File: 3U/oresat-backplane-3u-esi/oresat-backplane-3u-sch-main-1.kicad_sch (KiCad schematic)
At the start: 30 parts

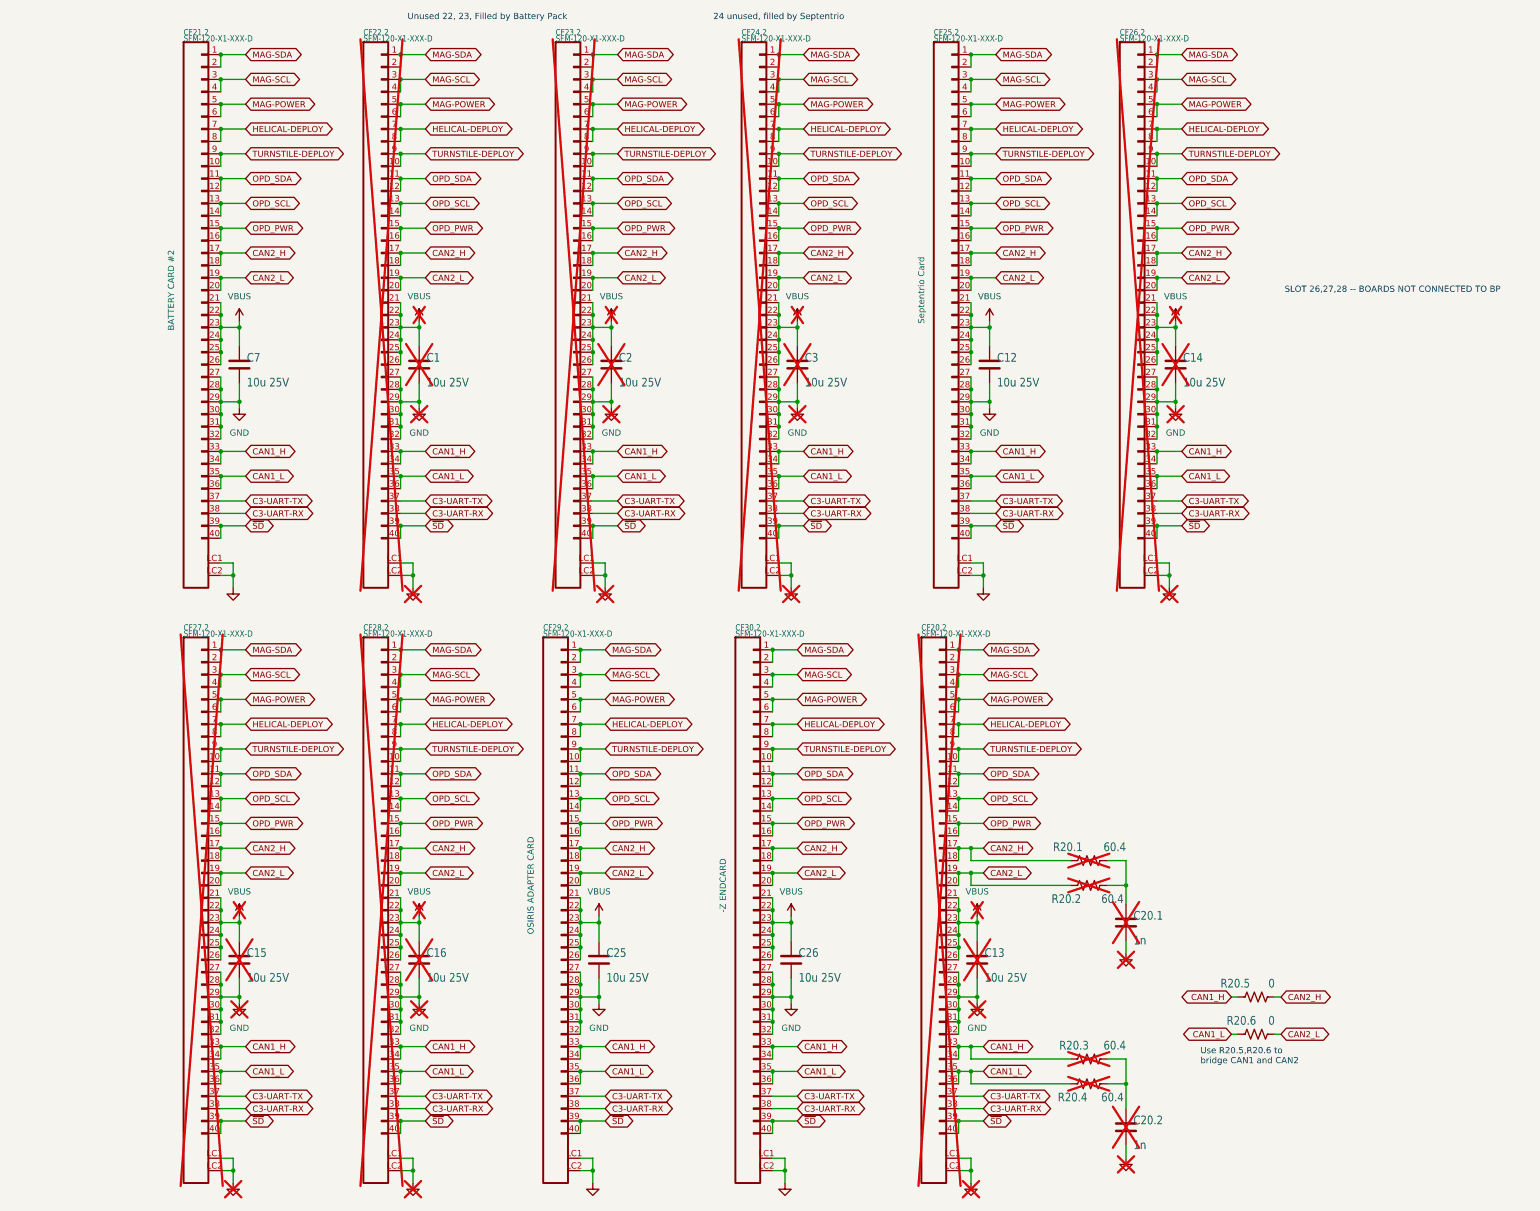
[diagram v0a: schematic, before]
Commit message: Added schematic and board variables, polished some silkscreen, reviewed board, renamed directory
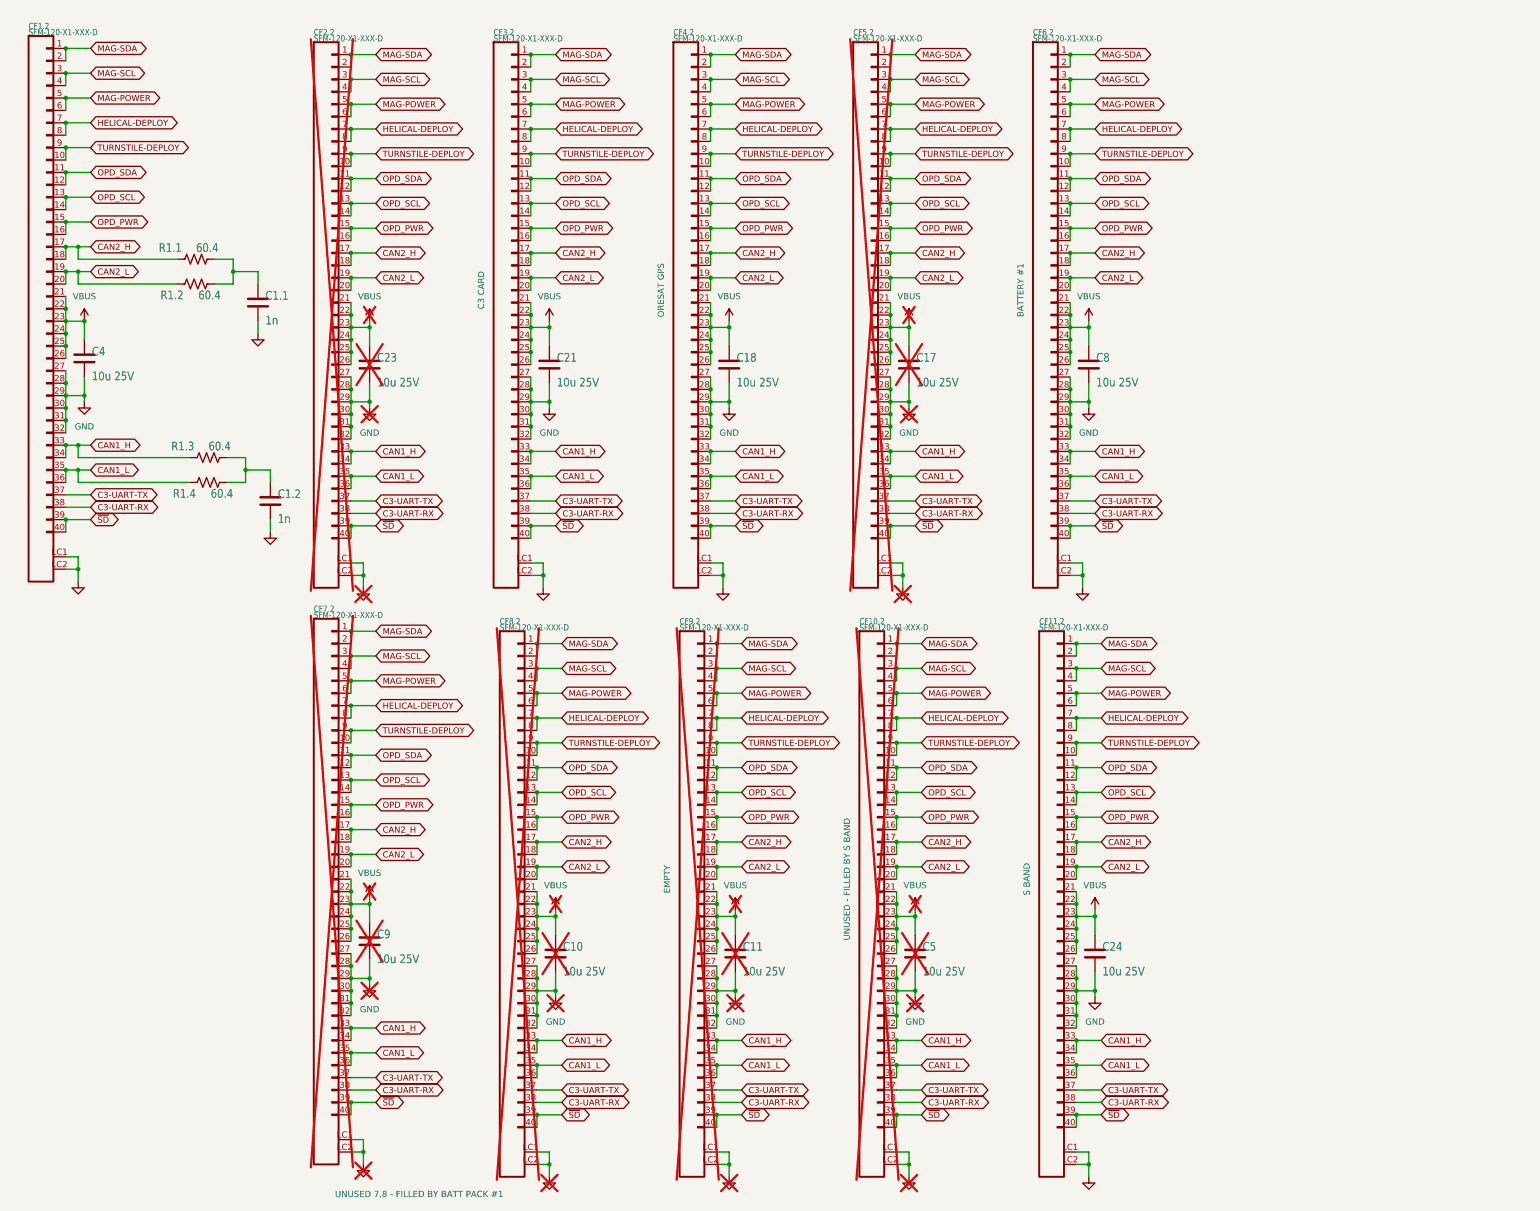
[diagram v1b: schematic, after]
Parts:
- removed C1, C12, C13, C14, C15, C16, C2, C25, C26, C3, C7: 10u 25V, Capacitor_SMD:C_1206_3216Metric, symbol Device:C
- removed C20.1, C20.2: 1n, oresat-passives:0603-C-NOSILK, symbol Device:C
- removed CF20.2, CF21.2, CF22.2, CF23.2, CF24.2, CF25.2, CF26.2, CF27.2, CF28.2, CF29.2, CF30.2: SFM-120-X1-XXX-D, oresat-connectors:J-SAMTEC-SFM-120-X1-XXX-D, symbol oresat-connectors:J-SAMTEC-SFM-120-X1-XXX-D
- removed R20.1, R20.2, R20.3, R20.4: 60.4, Resistor_SMD:R_1206_3216Metric, symbol Device:R_US
- removed R20.5, R20.6: 0, oresat-passives:0603-C-NOSILK, symbol Device:R_US
- added C1.1, C1.2: 1n, oresat-passives:0603-C-NOSILK, symbol Device:C
- added C10, C11, C17, C18, C21, C23, C24, C4, C5, C8, C9: 10u 25V, Capacitor_SMD:C_1206_3216Metric, symbol Device:C
- added CF1.2, CF10.2, CF11.2, CF2.2, CF3.2, CF4.2, CF5.2, CF6.2, CF7.2, CF8.2, CF9.2: SFM-120-X1-XXX-D, oresat-connectors:J-SAMTEC-SFM-120-X1-XXX-D, symbol oresat-connectors:J-SAMTEC-SFM-120-X1-XXX-D
- added R1.1, R1.2, R1.3, R1.4: 60.4, Resistor_SMD:R_1206_3216Metric, symbol Device:R_US
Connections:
- net C3-UART-RX: now also CF1.2.38, CF10.2.38, CF11.2.38, CF2.2.38, CF3.2.38, CF4.2.38, CF5.2.38, CF6.2.38, CF7.2.38, CF8.2.38, CF9.2.38
- net C3-UART-TX: now also CF1.2.37, CF10.2.37, CF11.2.37, CF2.2.37, CF3.2.37, CF4.2.37, CF5.2.37, CF6.2.37, CF7.2.37, CF8.2.37, CF9.2.37
- net CAN1_H: now also CF1.2.33, CF1.2.34, CF10.2.33, CF10.2.34, CF11.2.33, CF11.2.34, CF2.2.33, CF2.2.34, CF3.2.33, CF3.2.34, CF4.2.33, CF4.2.34, CF5.2.33, CF5.2.34, CF6.2.33, CF6.2.34, CF7.2.33, CF7.2.34, CF8.2.33, CF8.2.34, CF9.2.33, CF9.2.34, R1.3.2
- net CAN1_L: now also CF1.2.35, CF1.2.36, CF10.2.35, CF10.2.36, CF11.2.35, CF11.2.36, CF2.2.35, CF2.2.36, CF3.2.35, CF3.2.36, CF4.2.35, CF4.2.36, CF5.2.35, CF5.2.36, CF6.2.35, CF6.2.36, CF7.2.35, CF7.2.36, CF8.2.35, CF8.2.36, CF9.2.35, CF9.2.36, R1.4.1
- net CAN2_H: now also CF1.2.17, CF1.2.18, CF10.2.17, CF10.2.18, CF11.2.17, CF11.2.18, CF2.2.17, CF2.2.18, CF3.2.17, CF3.2.18, CF4.2.17, CF4.2.18, CF5.2.17, CF5.2.18, CF6.2.17, CF6.2.18, CF7.2.17, CF7.2.18, CF8.2.17, CF8.2.18, CF9.2.17, CF9.2.18, R1.1.2
- net CAN2_L: now also CF1.2.19, CF1.2.20, CF10.2.19, CF10.2.20, CF11.2.19, CF11.2.20, CF2.2.19, CF2.2.20, CF3.2.19, CF3.2.20, CF4.2.19, CF4.2.20, CF5.2.19, CF5.2.20, CF6.2.19, CF6.2.20, CF7.2.19, CF7.2.20, CF8.2.19, CF8.2.20, CF9.2.19, CF9.2.20, R1.2.1
- net GND: now also C1.1.2, C1.2.2, C10.2, C11.2, C17.2, C18.2, C21.2, C23.2, C24.2, C4.2, C5.2, C8.2, C9.2, CF1.2.27, CF1.2.28, CF1.2.29, CF1.2.30, CF1.2.31, CF1.2.32, CF1.2.LC1, CF1.2.LC2, CF10.2.27, CF10.2.28, CF10.2.29, CF10.2.30, CF10.2.31, CF10.2.32, CF10.2.LC1, CF10.2.LC2, CF11.2.27, CF11.2.28, CF11.2.29, CF11.2.30, CF11.2.31, CF11.2.32, CF11.2.LC1, CF11.2.LC2, CF2.2.27, CF2.2.28, CF2.2.29, CF2.2.30, CF2.2.31, CF2.2.32, CF2.2.LC1, CF2.2.LC2, CF3.2.27, CF3.2.28, CF3.2.29, CF3.2.30, CF3.2.31, CF3.2.32, CF3.2.LC1, CF3.2.LC2, CF4.2.27, CF4.2.28, CF4.2.29, CF4.2.30, CF4.2.31, CF4.2.32, CF4.2.LC1, CF4.2.LC2, CF5.2.27, CF5.2.28, CF5.2.29, CF5.2.30, CF5.2.31, CF5.2.32, CF5.2.LC1, CF5.2.LC2, CF6.2.27, CF6.2.28, CF6.2.29, CF6.2.30, CF6.2.31, CF6.2.32, CF6.2.LC1, CF6.2.LC2, CF7.2.27, CF7.2.28, CF7.2.29, CF7.2.30, CF7.2.31, CF7.2.32, CF7.2.LC1, CF7.2.LC2, CF8.2.27, CF8.2.28, CF8.2.29, CF8.2.30, CF8.2.31, CF8.2.32, CF8.2.LC1, CF8.2.LC2, CF9.2.27, CF9.2.28, CF9.2.29, CF9.2.30, CF9.2.31, CF9.2.32, CF9.2.LC1, CF9.2.LC2
- net HELICAL-DEPLOY: now also CF1.2.7, CF1.2.8, CF10.2.7, CF10.2.8, CF11.2.7, CF11.2.8, CF2.2.7, CF2.2.8, CF3.2.7, CF3.2.8, CF4.2.7, CF4.2.8, CF5.2.7, CF5.2.8, CF6.2.7, CF6.2.8, CF7.2.7, CF7.2.8, CF8.2.7, CF8.2.8, CF9.2.7, CF9.2.8
- net MAG-POWER: now also CF1.2.5, CF1.2.6, CF10.2.5, CF10.2.6, CF11.2.5, CF11.2.6, CF2.2.5, CF2.2.6, CF3.2.5, CF3.2.6, CF4.2.5, CF4.2.6, CF5.2.5, CF5.2.6, CF6.2.5, CF6.2.6, CF7.2.5, CF7.2.6, CF8.2.5, CF8.2.6, CF9.2.5, CF9.2.6
- net MAG-SCL: now also CF1.2.3, CF1.2.4, CF10.2.3, CF10.2.4, CF11.2.3, CF11.2.4, CF2.2.3, CF2.2.4, CF3.2.3, CF3.2.4, CF4.2.3, CF4.2.4, CF5.2.3, CF5.2.4, CF6.2.3, CF6.2.4, CF7.2.3, CF7.2.4, CF8.2.3, CF8.2.4, CF9.2.3, CF9.2.4
- net MAG-SDA: now also CF1.2.1, CF1.2.2, CF10.2.1, CF10.2.2, CF11.2.1, CF11.2.2, CF2.2.1, CF2.2.2, CF3.2.1, CF3.2.2, CF4.2.1, CF4.2.2, CF5.2.1, CF5.2.2, CF6.2.1, CF6.2.2, CF7.2.1, CF7.2.2, CF8.2.1, CF8.2.2, CF9.2.1, CF9.2.2
- net OPD_PWR: now also CF1.2.15, CF1.2.16, CF10.2.15, CF10.2.16, CF11.2.15, CF11.2.16, CF2.2.15, CF2.2.16, CF3.2.15, CF3.2.16, CF4.2.15, CF4.2.16, CF5.2.15, CF5.2.16, CF6.2.15, CF6.2.16, CF7.2.15, CF7.2.16, CF8.2.15, CF8.2.16, CF9.2.15, CF9.2.16
- net OPD_SCL: now also CF1.2.13, CF1.2.14, CF10.2.13, CF10.2.14, CF11.2.13, CF11.2.14, CF2.2.13, CF2.2.14, CF3.2.13, CF3.2.14, CF4.2.13, CF4.2.14, CF5.2.13, CF5.2.14, CF6.2.13, CF6.2.14, CF7.2.13, CF7.2.14, CF8.2.13, CF8.2.14, CF9.2.13, CF9.2.14
- net OPD_SDA: now also CF1.2.11, CF1.2.12, CF10.2.11, CF10.2.12, CF11.2.11, CF11.2.12, CF2.2.11, CF2.2.12, CF3.2.11, CF3.2.12, CF4.2.11, CF4.2.12, CF5.2.11, CF5.2.12, CF6.2.11, CF6.2.12, CF7.2.11, CF7.2.12, CF8.2.11, CF8.2.12, CF9.2.11, CF9.2.12
- net TURNSTILE-DEPLOY: now also CF1.2.10, CF1.2.9, CF10.2.10, CF10.2.9, CF11.2.10, CF11.2.9, CF2.2.10, CF2.2.9, CF3.2.10, CF3.2.9, CF4.2.10, CF4.2.9, CF5.2.10, CF5.2.9, CF6.2.10, CF6.2.9, CF7.2.10, CF7.2.9, CF8.2.10, CF8.2.9, CF9.2.10, CF9.2.9
- net VBUS: now also C10.1, C11.1, C17.1, C18.1, C21.1, C23.1, C24.1, C4.1, C5.1, C8.1, C9.1, CF1.2.21, CF1.2.22, CF1.2.23, CF1.2.24, CF1.2.25, CF1.2.26, CF10.2.21, CF10.2.22, CF10.2.23, CF10.2.24, CF10.2.25, CF10.2.26, CF11.2.21, CF11.2.22, CF11.2.23, CF11.2.24, CF11.2.25, CF11.2.26, CF2.2.21, CF2.2.22, CF2.2.23, CF2.2.24, CF2.2.25, CF2.2.26, CF3.2.21, CF3.2.22, CF3.2.23, CF3.2.24, CF3.2.25, CF3.2.26, CF4.2.21, CF4.2.22, CF4.2.23, CF4.2.24, CF4.2.25, CF4.2.26, CF5.2.21, CF5.2.22, CF5.2.23, CF5.2.24, CF5.2.25, CF5.2.26, CF6.2.21, CF6.2.22, CF6.2.23, CF6.2.24, CF6.2.25, CF6.2.26, CF7.2.21, CF7.2.22, CF7.2.23, CF7.2.24, CF7.2.25, CF7.2.26, CF8.2.21, CF8.2.22, CF8.2.23, CF8.2.24, CF8.2.25, CF8.2.26, CF9.2.21, CF9.2.22, CF9.2.23, CF9.2.24, CF9.2.25, CF9.2.26
- net ~{SD}: now also CF1.2.39, CF1.2.40, CF10.2.39, CF10.2.40, CF11.2.39, CF11.2.40, CF2.2.39, CF2.2.40, CF3.2.39, CF3.2.40, CF4.2.39, CF4.2.40, CF5.2.39, CF5.2.40, CF6.2.39, CF6.2.40, CF7.2.39, CF7.2.40, CF8.2.39, CF8.2.40, CF9.2.39, CF9.2.40
- new net: C1.1.1, R1.1.1, R1.2.2
- new net: C1.2.1, R1.3.1, R1.4.2
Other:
- note added: "UNUSED 7,8 - FILLED BY BATT PACK #1"
- note removed: "24 unused, filled by Septentrio"
- note removed: "SLOT 26,27,28 -- BOARDS NOT CONNECTED TO BP"
- note removed: "Unused 22, 23, Filled by Battery Pack"
- note removed: "Use R20.5,R20.6 to bridge CAN1 and CAN2"
- company: Portland State Aerospace Society -> PSAS / ESI
- title: Generic OreSat 3U Backplane -> OreSat 3U Backplane for ESI

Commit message: Labelled connectors & disconnected C3 LBand
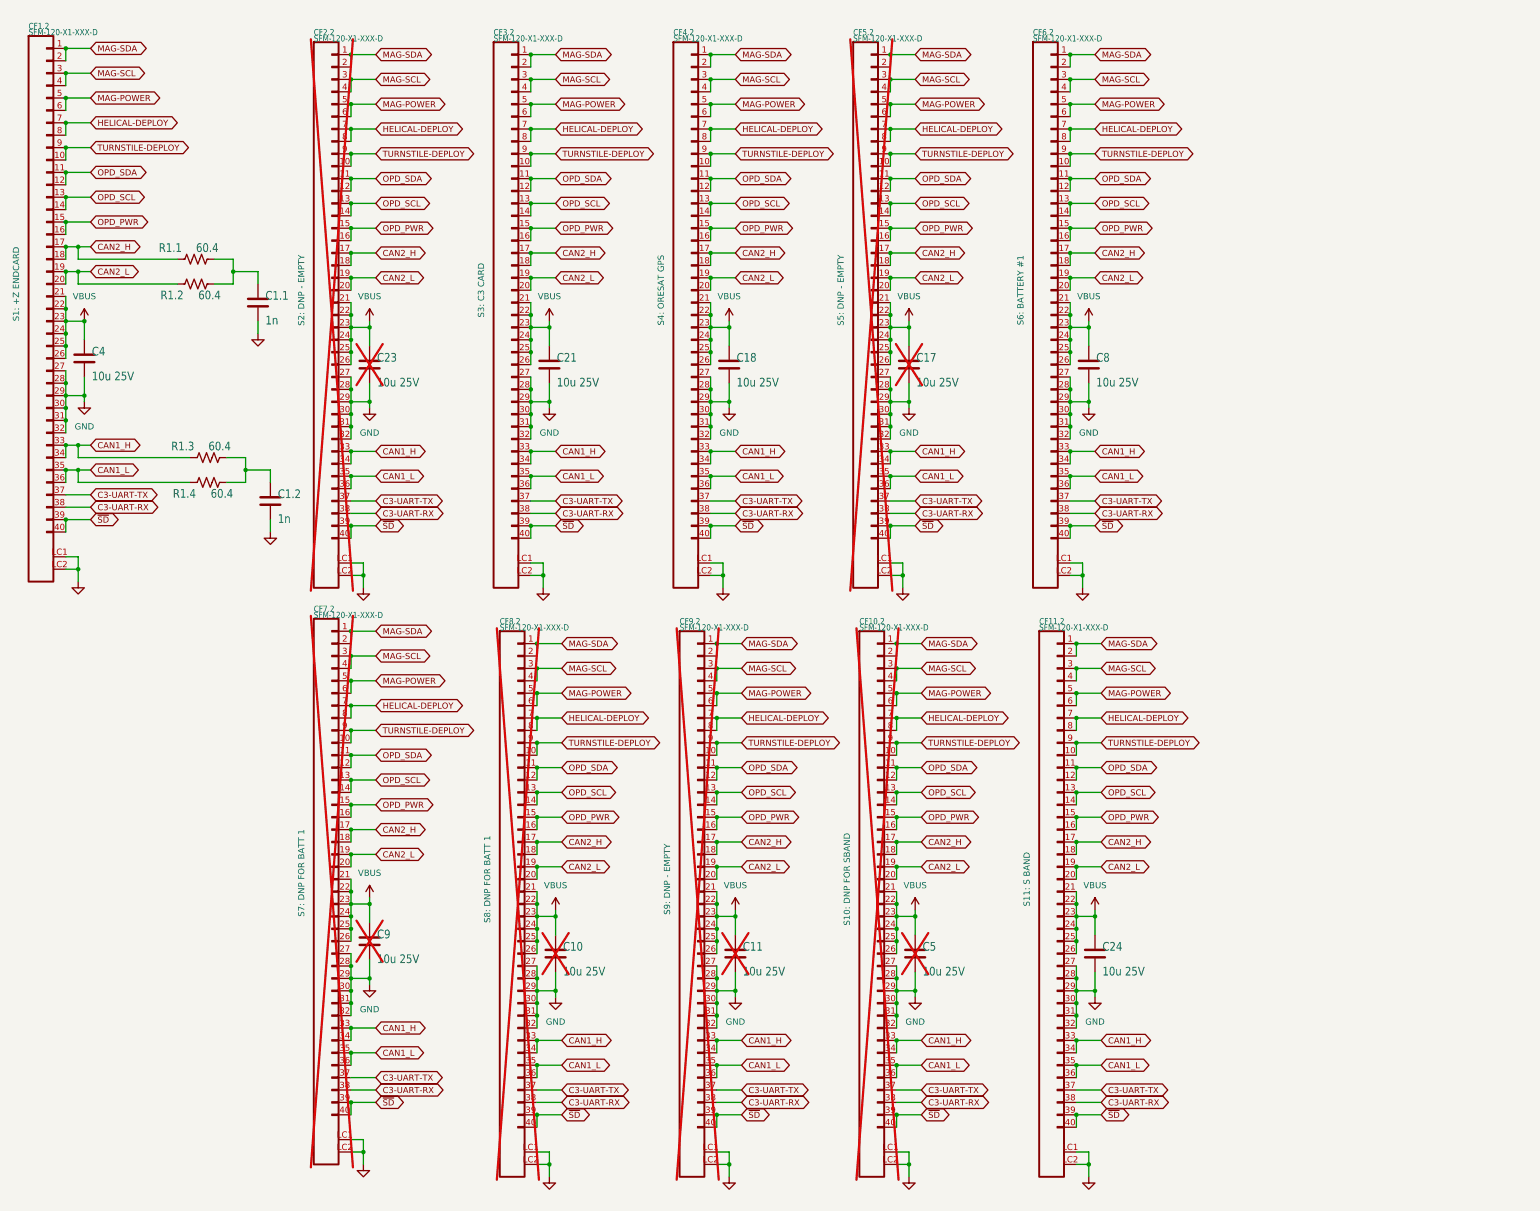
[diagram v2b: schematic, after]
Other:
- note removed: "UNUSED 7,8 - FILLED BY BATT PACK #1"
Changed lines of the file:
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@@
 		(company "PSAS / ESI")
 	)
-	(text "UNUSED 7,8 - FILLED BY BATT PACK #1\n"
-		(exclude_from_sim no)
-		(at 181.61 260.35 0)
-		(effects
-			(font
-				(size 1.27 1.27)
-			)
-		)
-	)
 	(junction
 		(at 204.47 87.63)
@@
 		(in_bom yes)
 		(on_board yes)
-		(dnp yes)
+		(dnp no)
 		(fields_autoplaced yes)
 		(property "Reference" "#PWR07"
@@
 		(in_bom yes)
 		(on_board yes)
-		(dnp yes)
+		(dnp no)
 		(fields_autoplaced yes)
 		(property "Reference" "#VBUS02"
@@
 			)
 		)
-		(property "Description" "EMPTY"
+		(property "Description" "S9: DNP - EMPTY"
 			(at 232.41 195.58 90)
 			(effects
@@
 		(in_bom yes)
 		(on_board yes)
-		(dnp yes)
+		(dnp no)
 		(fields_autoplaced yes)
 		(property "Reference" "#VBUS06"
@@
 			)
 		)
-		(property "Description" "BATTERY #1"
+		(property "Description" "S6: BATTERY #1"
 			(at 304.8 74.93 90)
 			(effects
@@
 			)
 		)
-		(property "Description" ""
-			(at 162.56 74.93 0)
+		(property "Description" "S2: DNP - EMPTY"
+			(at 157.48 74.93 90)
 			(effects
 				(font
@@
 		(in_bom yes)
 		(on_board yes)
-		(dnp yes)
+		(dnp no)
 		(fields_autoplaced yes)
 		(property "Reference" "#VBUS011"
@@
 		(in_bom yes)
 		(on_board yes)
-		(dnp yes)
+		(dnp no)
 		(fields_autoplaced yes)
 		(property "Reference" "#VBUS09"
@@
 		(in_bom yes)
 		(on_board yes)
-		(dnp yes)
+		(dnp no)
 		(property "Reference" "#GND0103"
 			(at 281.94 256.54 0)
@@
 		(in_bom yes)
 		(on_board yes)
-		(dnp yes)
+		(dnp no)
 		(property "Reference" "#GND0112"
 			(at 280.67 135.89 0)
@@
 			)
 		)
-		(property "Description" "S BAND"
+		(property "Description" "S11: S BAND"
 			(at 306.07 195.58 90)
 			(effects
@@
 		(in_bom yes)
 		(on_board yes)
-		(dnp yes)
+		(dnp no)
 		(property "Reference" "#GND0123"
 			(at 245.11 256.54 0)
@@
 		(in_bom yes)
 		(on_board yes)
-		(dnp yes)
+		(dnp no)
 		(property "Reference" "#GND0101"
 			(at 170.18 135.89 0)
@@
 			)
 		)
-		(property "Description" ""
-			(at 104.14 73.66 0)
+		(property "Description" "S1: +Z ENDCARD"
+			(at 99.06 73.66 90)
 			(effects
 				(font
@@
 			)
 		)
-		(property "Description" "UNUSED - FILLED BY S BAND"
+		(property "Description" "S10: DNP FOR SBAND"
 			(at 269.24 195.58 90)
 			(effects
@@
 			)
 		)
-		(property "Description" "ORESAT GPS"
+		(property "Description" "S4: ORESAT GPS"
 			(at 231.14 74.93 90)
 			(effects
@@
 		(in_bom yes)
 		(on_board yes)
-		(dnp yes)
+		(dnp no)
 		(fields_autoplaced yes)
 		(property "Reference" "#PWR08"
@@
 			)
 		)
-		(property "Description" ""
-			(at 200.66 195.58 0)
+		(property "Description" "S8: DNP FOR BATT 1"
+			(at 195.58 195.58 90)
 			(effects
 				(font
@@
 		(in_bom yes)
 		(on_board yes)
-		(dnp yes)
+		(dnp no)
 		(property "Reference" "#GND0120"
 			(at 208.28 256.54 0)
@@
 		(in_bom yes)
 		(on_board yes)
-		(dnp yes)
+		(dnp no)
 		(fields_autoplaced yes)
 		(property "Reference" "#PWR02"
@@
 		(in_bom yes)
 		(on_board yes)
-		(dnp yes)
+		(dnp no)
 		(fields_autoplaced yes)
 		(property "Reference" "#VBUS01"
@@
 			)
 		)
-		(property "Description" ""
-			(at 162.56 193.04 0)
+		(property "Description" "S7: DNP FOR BATT 1"
+			(at 157.48 194.31 90)
 			(effects
 				(font
@@
 		(in_bom yes)
 		(on_board yes)
-		(dnp yes)
+		(dnp no)
 		(fields_autoplaced yes)
 		(property "Reference" "#PWR06"
@@
 		(in_bom yes)
 		(on_board yes)
-		(dnp yes)
+		(dnp no)
 		(property "Reference" "#GND0114"
 			(at 170.18 254 0)
@@
 			)
 		)
-		(property "Description" "C3 CARD"
+		(property "Description" "S3: C3 CARD"
 			(at 194.31 74.93 90)
 			(effects
@@
 		(in_bom yes)
 		(on_board yes)
-		(dnp yes)
+		(dnp no)
 		(fields_autoplaced yes)
 		(property "Reference" "#PWR05"
@@
 		(in_bom yes)
 		(on_board yes)
-		(dnp yes)
+		(dnp no)
 		(fields_autoplaced yes)
 		(property "Reference" "#VBUS03"
@@
 		(in_bom yes)
 		(on_board yes)
-		(dnp yes)
+		(dnp no)
 		(fields_autoplaced yes)
 		(property "Reference" "#PWR031"
@@
 			)
 		)
-		(property "Description" ""
-			(at 273.05 74.93 0)
+		(property "Description" "S5: DNP - EMPTY"
+			(at 267.97 74.93 90)
 			(effects
 				(font
